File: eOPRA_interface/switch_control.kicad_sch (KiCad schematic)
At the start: 111 parts, among them Q1 G3VM-351VY1-TR05, Q11 G3VM-351VY1-TR05, Q14 G3VM-351VY1-TR05, Q15 G3VM-351VY1-TR05, Q17 G3VM-351VY1-TR05, Q18 G3VM-351VY1-TR05, Q20 G3VM-351VY1-TR05, Q22 G3VM-351VY1-TR05, Q23 G3VM-351VY1-TR05, Q26 G3VM-351VY1-TR05, Q27 G3VM-351VY1-TR05, Q30 G3VM-351VY1-TR05, Q31 G3VM-351VY1-TR05, Q34 G3VM-351VY1-TR05, Q7 G3VM-351VY1-TR05, Q7 RU1J002YNTCL, Q9 G3VM-351VY1-TR05

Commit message: initial state
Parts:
- added Q7: RU1J002YNTCL, 1_Semi_TO_SOT:SOT-323FL, symbol 1.semi.discrete:Q_NMOS_GSD
- added R49: 10k, 2_Passives_Resistors_SMD_IPC:R_1608_603_B, symbol 2.passive:R
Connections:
- net GNDREF: now also Q7.2 (S), R49.1; no longer D3.1 (K)
- new net: D3.1 (K), Q7.3 (D)
- new net SWITCH_CTL: Q7.1 (G), R49.2
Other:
- note added: "CONSIDER REPLACEMENT TO G3VM-351GL"
- moved on the sheet: D3, R17, SW4, TP5, U17

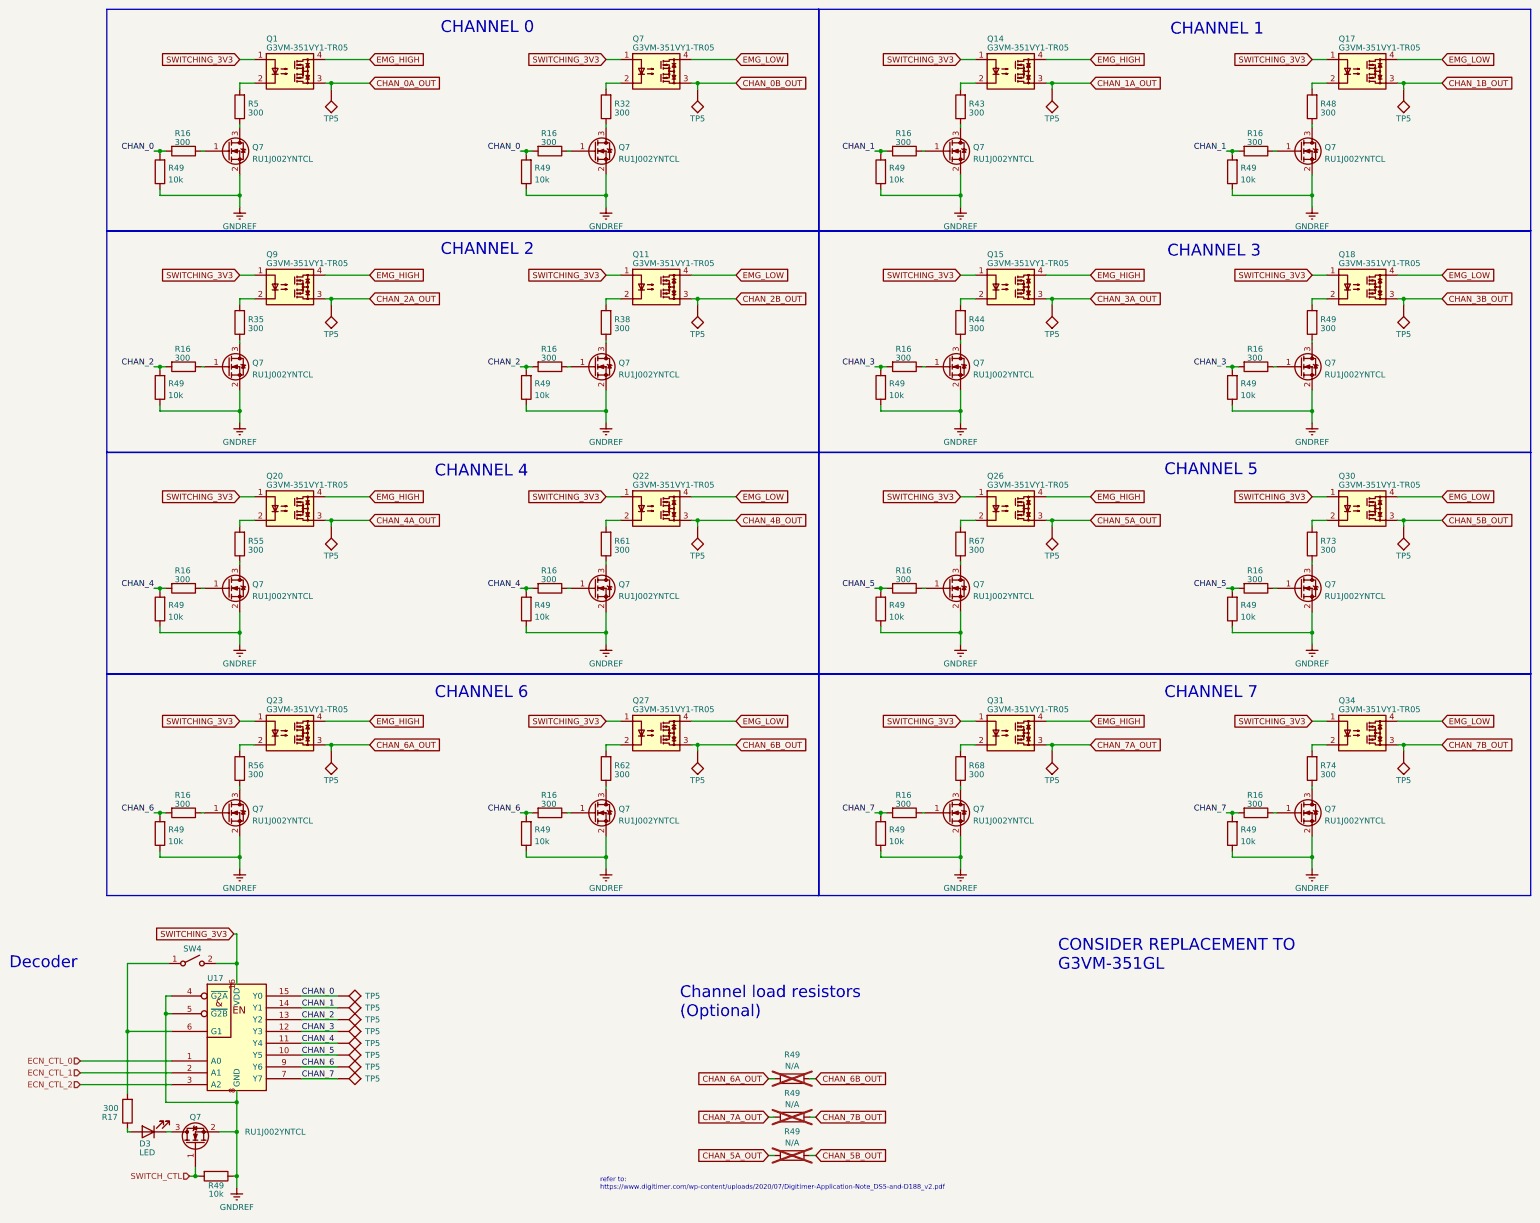
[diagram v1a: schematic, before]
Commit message: switch port on interrupt
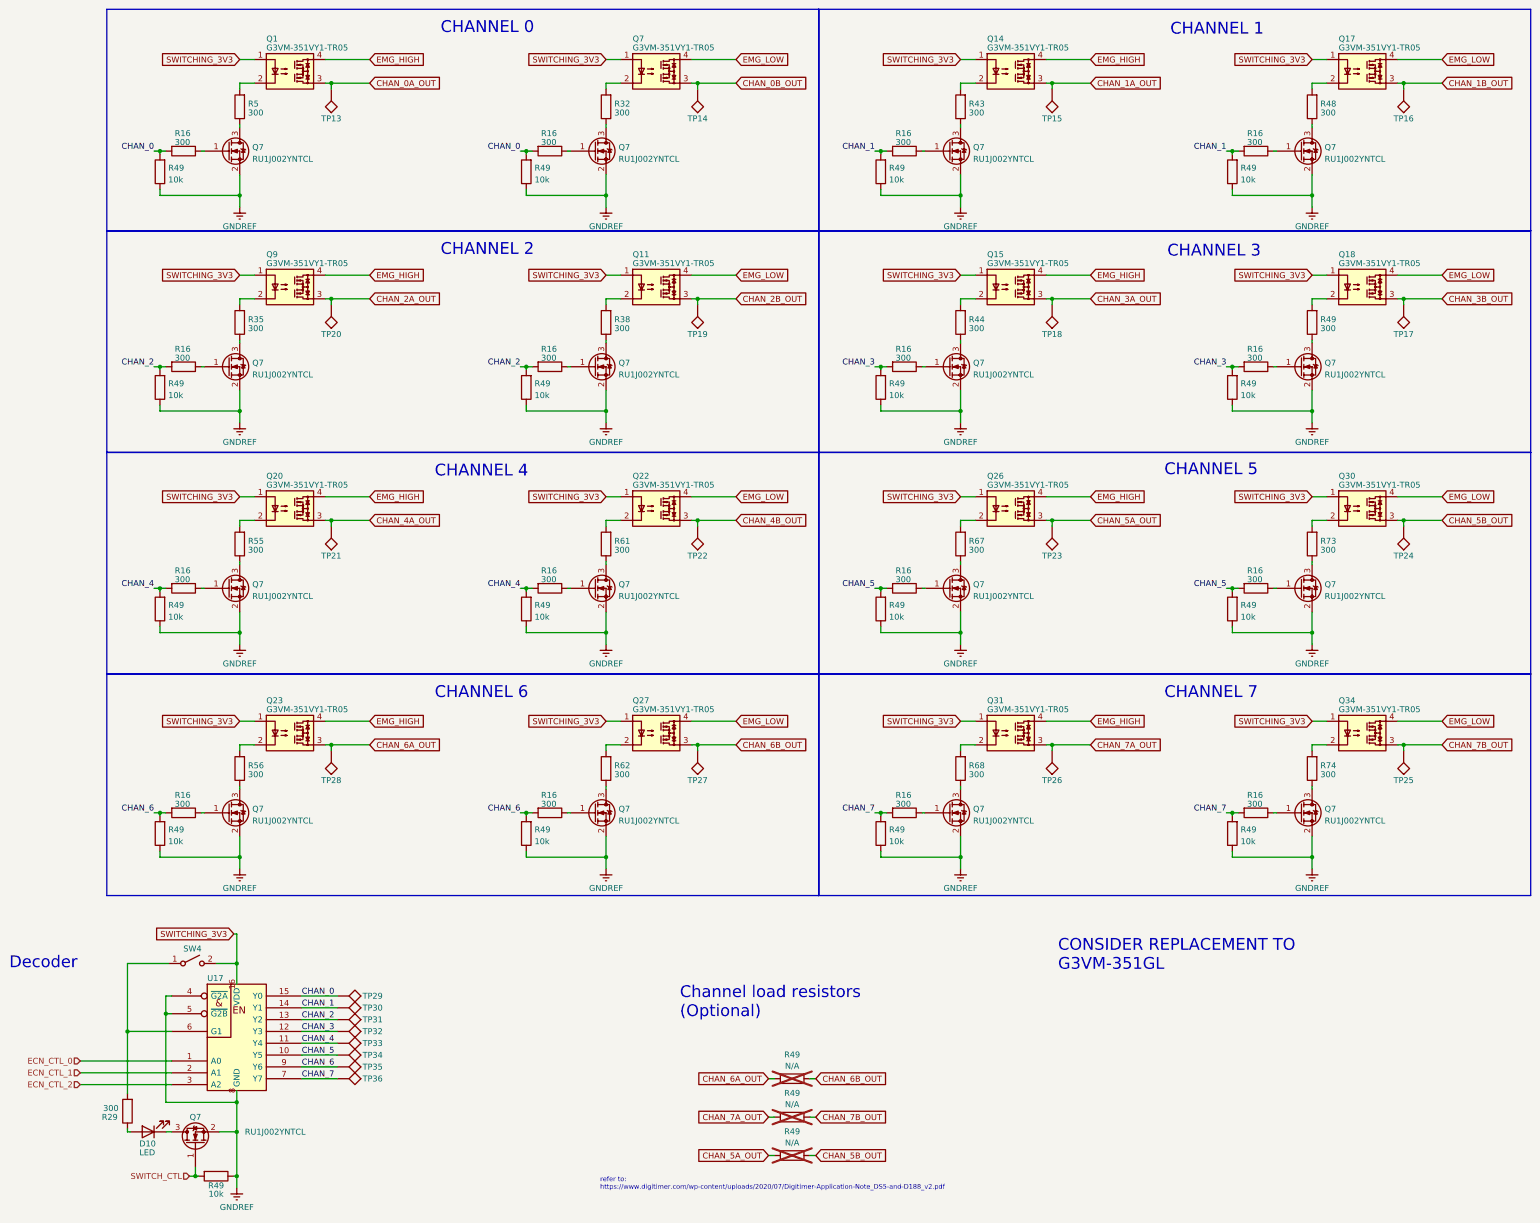
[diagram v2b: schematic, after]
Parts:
- renumbered D3 to D10, R17 to R29, TP5 to TP13, TP5 to TP14, TP5 to TP15, TP5 to TP16, TP5 to TP17, TP5 to TP18, TP5 to TP19, TP5 to TP20, TP5 to TP21, TP5 to TP22, TP5 to TP23, TP5 to TP24, TP5 to TP25, TP5 to TP26, TP5 to TP27, TP5 to TP28, TP5 to TP29, TP5 to TP30, TP5 to TP31, TP5 to TP32, TP5 to TP33, TP5 to TP34, TP5 to TP35, TP5 to TP36
